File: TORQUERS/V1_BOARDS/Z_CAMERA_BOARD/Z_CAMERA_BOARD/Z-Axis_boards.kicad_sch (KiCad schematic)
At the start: 36 parts, among them J1 0530470810, Q1 BSS138, Q2 BSS138, Q4 BSS138, Q5 BSS138, U1 DRV8830DGQ

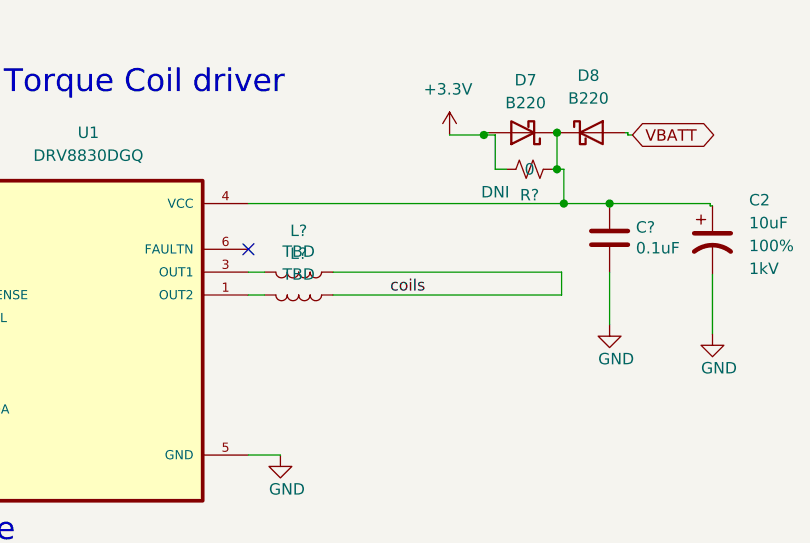
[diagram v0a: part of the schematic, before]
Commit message: Made changes to LTC ; remaining switches for H bridge and  LTC3130 for 70mm panel
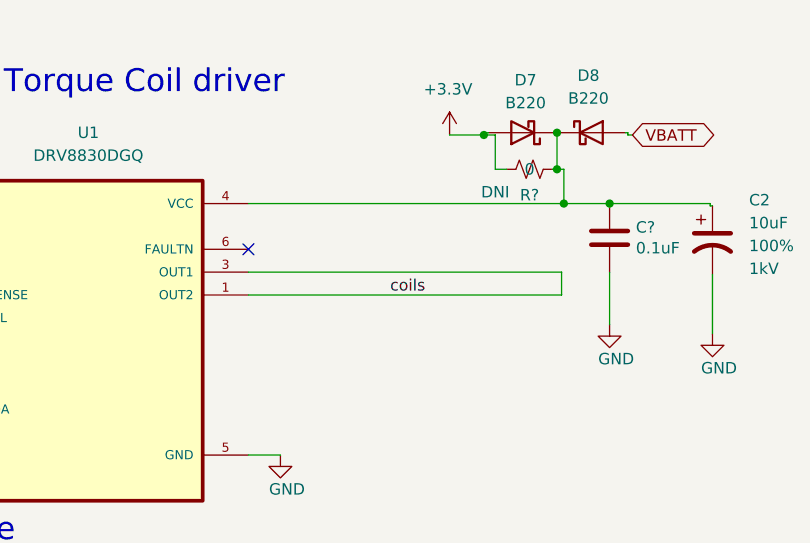
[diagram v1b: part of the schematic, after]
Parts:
- removed L? (x2): TBD, Inductor_SMD:L_0603_1608Metric, symbol Device:L
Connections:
- net coils: now also U1.1 (OUT2), U1.3 (OUT1)
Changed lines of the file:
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@@
     (stroke (width 0) (type default))
   )
-  (wire (pts (xy 214.376 41.91) (xy 216.154 41.91))
+  (wire (pts (xy 214.376 41.91) (xy 249.174 41.91))
     (stroke (width 0) (type default))
   )
@@
     (stroke (width 0) (type default))
   )
-  (wire (pts (xy 223.774 41.91) (xy 249.174 41.91))
-    (stroke (width 0) (type default))
-  )
   (wire (pts (xy 115.824 44.196) (xy 117.094 44.196))
     (stroke (width 0) (type default))
@@
     (stroke (width 0) (type default))
   )
-  (wire (pts (xy 214.376 44.45) (xy 216.154 44.45))
+  (wire (pts (xy 214.376 44.45) (xy 249.174 44.45))
     (stroke (width 0) (type default))
   )
@@
   )
   (wire (pts (xy 179.07 46.99) (xy 178.816 46.99))
-    (stroke (width 0) (type default))
-  )
-  (wire (pts (xy 249.174 44.45) (xy 223.774 44.45))
     (stroke (width 0) (type default))
   )
@@
         (path "/99e96bba-18e9-4e1a-93db-d36759d20919"
           (reference "R4") (unit 1)
-        )
-      )
-    )
-  )
-  (symbol (lib_id "Device:L") (at 219.964 44.45 270) (unit 1)
-    (in_bom yes) (on_board yes) (dnp no)
-    (property "Reference" "L?" (at 219.964 39.8526 90)
-      (effects (font (size 1.27 1.27)))
-    )
-    (property "Value" "TBD" (at 219.964 42.164 90)
-      (effects (font (size 1.27 1.27)))
-    )
-    (property "Footprint" "Inductor_SMD:L_0603_1608Metric" (at 219.964 44.45 0)
-      (effects (font (size 1.27 1.27)) hide)
-    )
-    (property "Datasheet" "~" (at 219.964 44.45 0)
-      (effects (font (size 1.27 1.27)) hide)
-    )
-    (pin "1")
-    (pin "2")
-    (instances
-      (project "xpanel"
-        (path "/30bf83b4-3f3b-46f2-ac0f-8077e2dc1b24"
-          (reference "L?") (unit 1)
-        )
-      )
-      (project "Xpanel_V0"
-        (path "/97119169-578f-44be-8822-faf8f0e4fcd6"
-          (reference "L2") (unit 1)
-        )
-      )
-      (project "Z-Axis_boards"
-        (path "/99e96bba-18e9-4e1a-93db-d36759d20919"
-          (reference "L2") (unit 1)
         )
       )
@@
         )
       )
-    )
-  )
-  (symbol (lib_id "Device:L") (at 219.964 41.91 270) (unit 1)
-    (in_bom yes) (on_board yes) (dnp no)
-    (property "Reference" "L?" (at 219.964 37.3126 90)
-      (effects (font (size 1.27 1.27)))
-    )
-    (property "Value" "TBD" (at 219.964 39.624 90)
-      (effects (font (size 1.27 1.27)))
-    )
-    (property "Footprint" "Inductor_SMD:L_0603_1608Metric" (at 219.964 41.91 0)
-      (effects (font (size 1.27 1.27)) hide)
-    )
-    (property "Datasheet" "~" (at 219.964 41.91 0)
-      (effects (font (size 1.27 1.27)) hide)
-    )
-    (pin "1")
-    (pin "2")
-    (instances
-      (project "xpanel"
-        (path "/30bf83b4-3f3b-46f2-ac0f-8077e2dc1b24"
-          (reference "L?") (unit 1)
-        )
-      )
-      (project "Xpanel_V0"
-        (path "/97119169-578f-44be-8822-faf8f0e4fcd6"
-          (reference "L1") (unit 1)
-        )
-      )
-      (project "Z-Axis_boards"
-        (path "/99e96bba-18e9-4e1a-93db-d36759d20919"
-          (reference "L1") (unit 1)
-        )
-      )
